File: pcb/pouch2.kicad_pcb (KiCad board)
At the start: 2 copper layers, 80 x 100 mm, 163 parts, among them J101 Conn_01x06_Male, J102 Conn_01x03_Male, J103 Conn_01x04_Male, J501 Conn_01x02_Male, J502 Conn_01x02_Male, J503 Conn_01x02_Male, J504 Conn_01x02_Male, J505 Conn_02x02_Odd_Even, J701 PiZero, J901 Conn_02x03_Counter_Clockwise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

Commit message: fixed missing GND-line to SD-Card-Adapter
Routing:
- net GND: track 320.0 -> 336.5 mm, vias 46 -> 49
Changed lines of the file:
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@@
+	)
+	(segment
+		(start 84.5 103.4)
+		(end 82.7 103.4)
+		(width 0.3)
+		(layer "F.Cu")
+		(net 119)
 	)
 	(segment
@@
 		(end 106.44 145.46)
 		(width 0.2)
+		(layer "F.Cu")
+		(net 119)
+	)
+	(segment
+		(start 82.294948 108.9)
+		(end 82.3 108.9)
+		(width 0.3)
 		(layer "F.Cu")
 		(net 119)
@@
 	)
 	(segment
+		(start 79.6 106.4)
+		(end 79.794948 106.4)
+		(width 0.3)
+		(layer "F.Cu")
+		(net 119)
+	)
+	(segment
 		(start 88.61 141.747057)
 		(end 88.61 140.21)
@@
 	)
 	(segment
+		(start 79.794948 106.4)
+		(end 82.294948 108.9)
+		(width 0.3)
+		(layer "F.Cu")
+		(net 119)
+	)
+	(segment
 		(start 114.06 148)
 		(end 112.81 146.75)
@@
 	)
 	(via
+		(at 82.7 103.4)
+		(size 0.6)
+		(drill 0.3)
+		(layers "F.Cu" "B.Cu")
+		(net 119)
+	)
+	(via
 		(at 110.227817 87.272183)
 		(size 0.6)
@@
 	)
 	(via
+		(at 82.3 108.9)
+		(size 0.6)
+		(drill 0.3)
+		(layers "F.Cu" "B.Cu")
+		(net 119)
+	)
+	(via
 		(at 128.75 140.8)
 		(size 0.6)
@@
 	(via
 		(at 94.4 70.8)
+		(size 0.6)
+		(drill 0.3)
+		(layers "F.Cu" "B.Cu")
+		(net 119)
+	)
+	(via
+		(at 79.6 106.4)
 		(size 0.6)
 		(drill 0.3)
@@
 	)
 	(segment
+		(start 82.3 108.9)
+		(end 82.59 109.19)
+		(width 0.3)
+		(layer "B.Cu")
+		(net 119)
+	)
+	(segment
+		(start 82.59 109.19)
+		(end 82.59 115.42)
+		(width 0.3)
+		(layer "B.Cu")
+		(net 119)
+	)
+	(segment
 		(start 113.8 69.95)
 		(end 113.8 70.7)
@@
 	)
 	(segment
+		(start 82.7 103.4)
+		(end 79.7 106.4)
+		(width 0.3)
+		(layer "B.Cu")
+		(net 119)
+	)
+	(segment
 		(start 123.2875 133.7)
 		(end 120.75 133.7)
@@
 		(layer "B.Cu")
 		(net 119)
+	)
+	(segment
+		(start 79.7 106.4)
+		(end 79.6 106.4)
+		(width 0.3)
+		(layer "B.Cu")
+		(net 119)

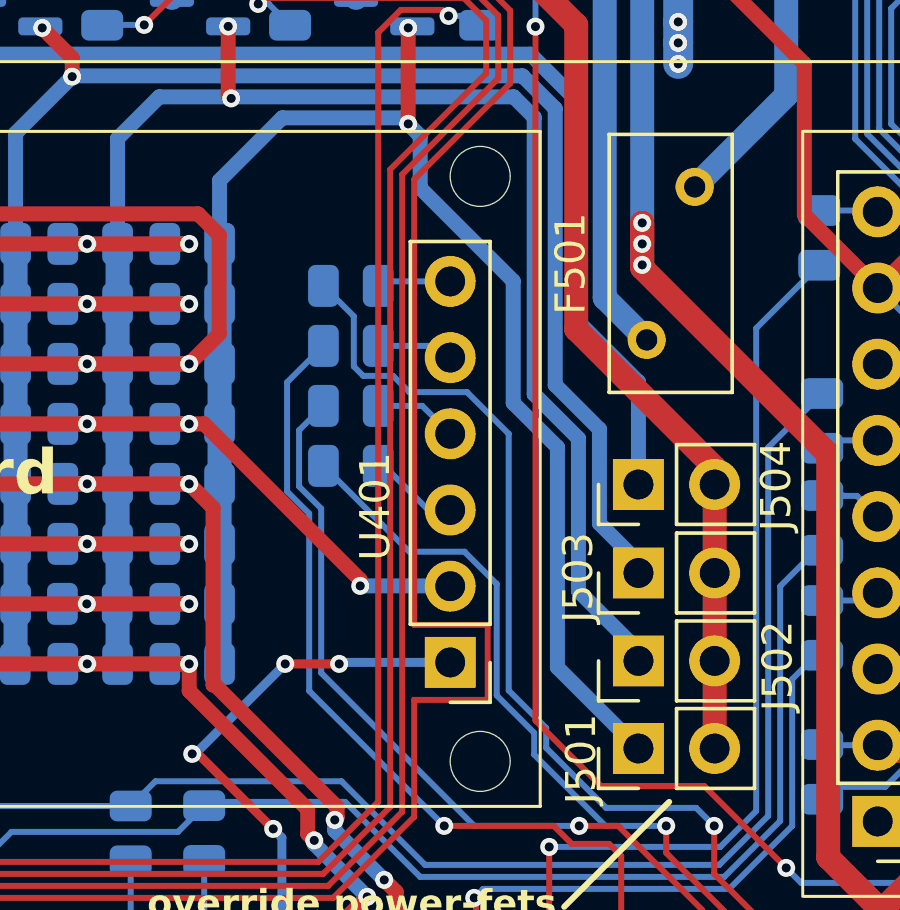
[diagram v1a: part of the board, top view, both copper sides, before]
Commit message: added capacitor for SD-Card
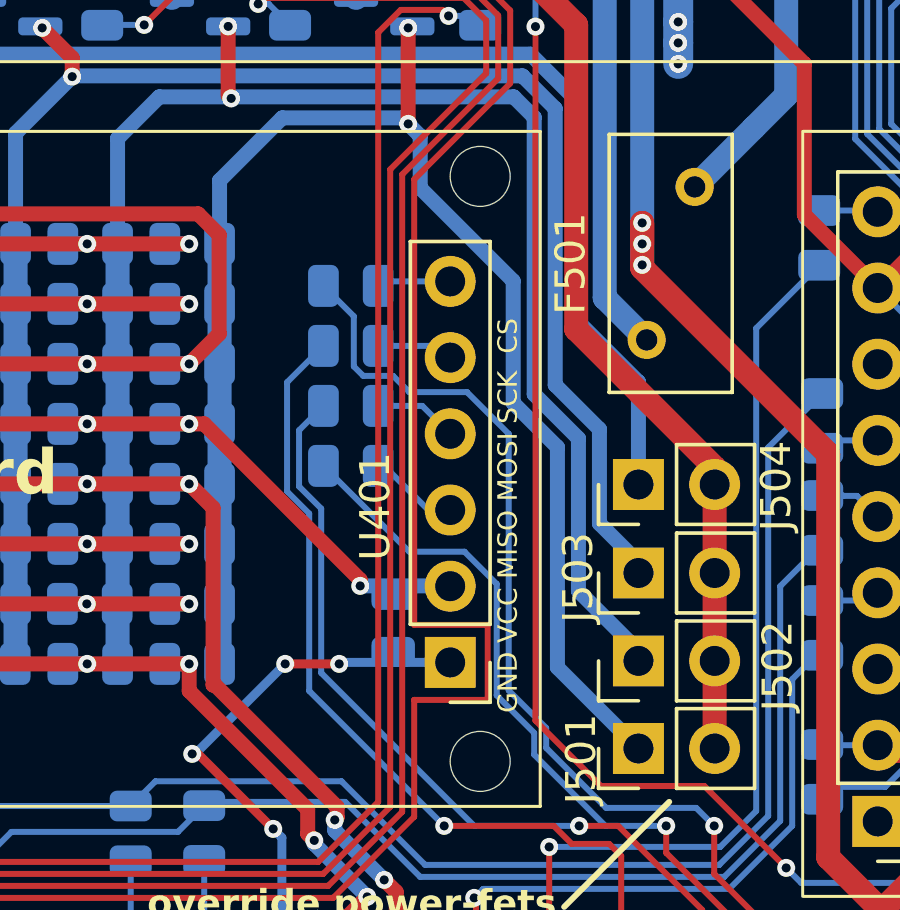
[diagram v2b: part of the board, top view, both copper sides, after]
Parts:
- added C401: C, Capacitor_SMD:C_0805_2012Metric, B.Cu at (86.3, 102.0)
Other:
- board text added: "GND VCC MISO MOSI SCK CS"
